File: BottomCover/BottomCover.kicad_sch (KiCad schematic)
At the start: 88 parts, among them J1 USB_C_Receptacle_USB2.0, J12 SM02B-SRSS-TB(LF)(SN), Q2 A03407, SW1 SW_PUSH, SW10 SW_PUSH, SW11 SW_PUSH, SW12 SW_PUSH, SW13 SW_PUSH, SW14 SW_PUSH, SW15 SW_PUSH, SW16 SW_PUSH, SW17 SW_PUSH, SW18 SW_PUSH, SW19 SW_PUSH, SW2 SW_PUSH, SW20 SW_PUSH, SW21 SW_PUSH, SW22 SW_PUSH, SW23 SW_PUSH, SW24 SW_PUSH, SW25 Rotary_Encoder_Switch, SW26 SW_PUSH, SW27 SW_PUSH, SW28 SW_PUSH, SW3 SW_PUSH, SW4 SW_PUSH, SW5 SW_PUSH, SW6 SW_PUSH, SW7 SW_PUSH, SW8 SW_PUSH, SW9 SW_PUSH, U1 LN2054Y42AMR, U2 E73-2G4M08S1C, U3 AP2112K-3.3, Y1 32.768kHz

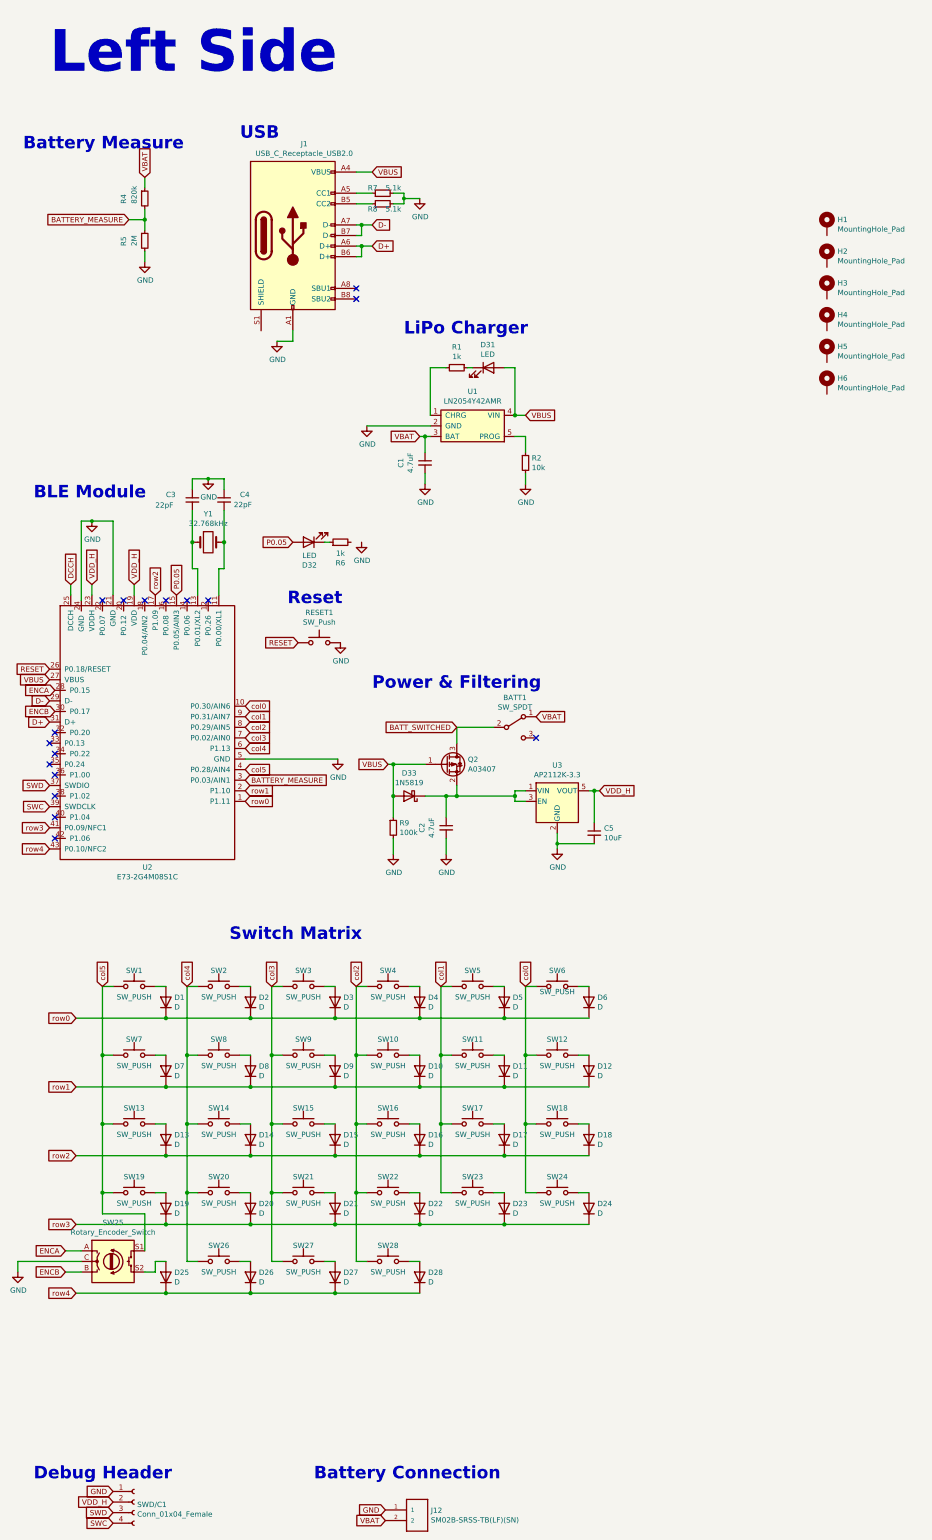
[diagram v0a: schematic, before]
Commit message: minor updates for SMD assembly
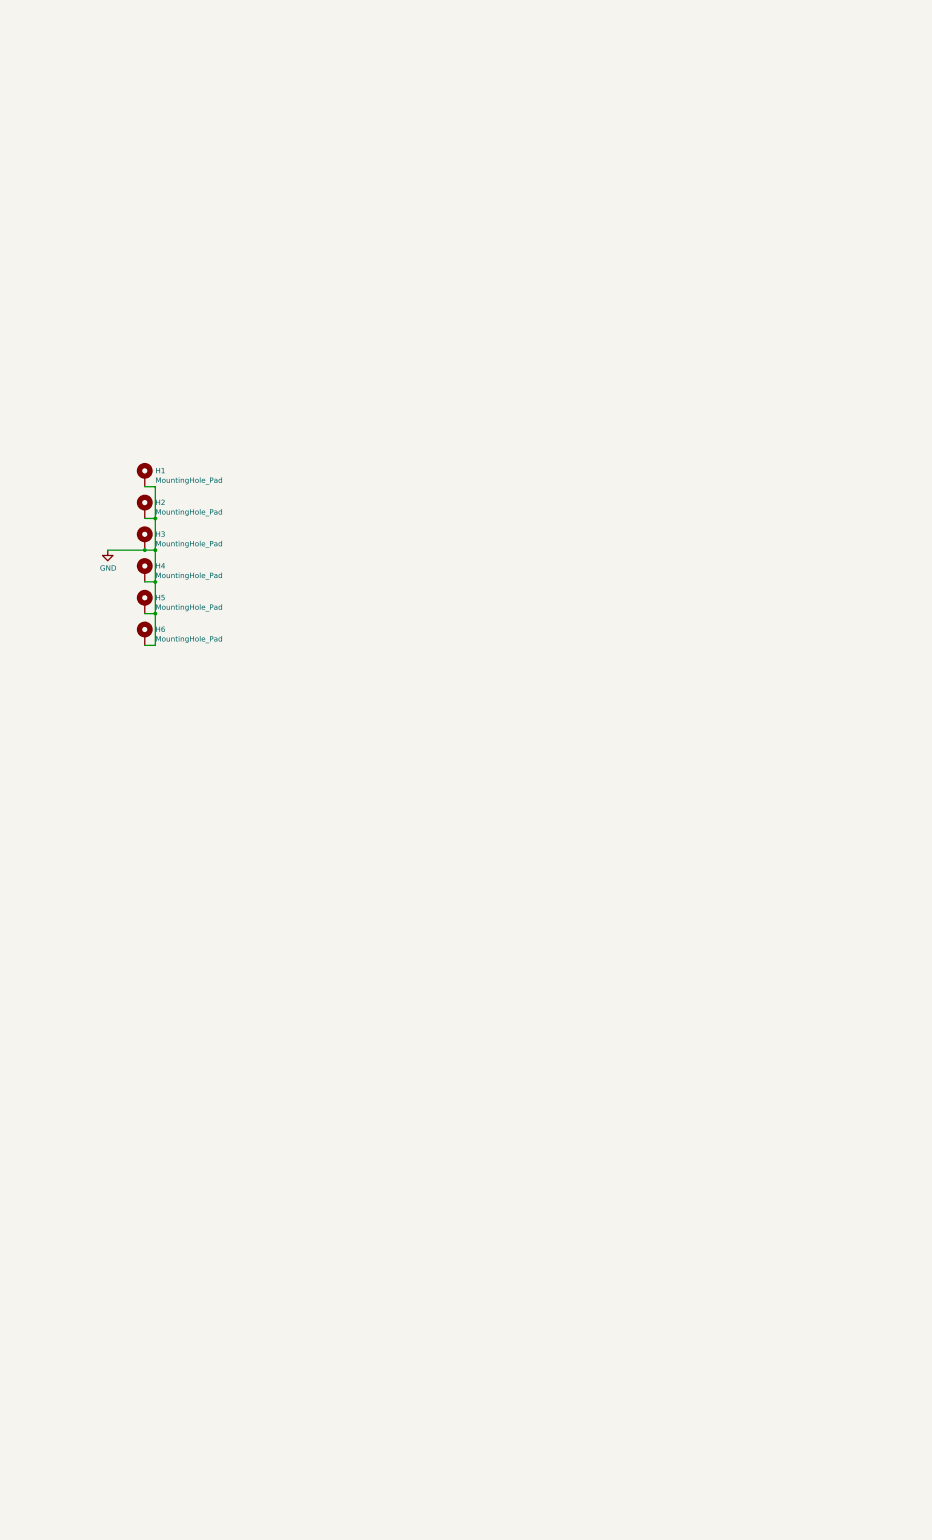
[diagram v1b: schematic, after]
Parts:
- removed BATT1: SW_SPDT, BlueSof:SW-TH_MSK12C02, symbol Switch:SW_SPDT
- removed C1, C2: 4.7uF, Capacitor_SMD:C_0603_1608Metric_Pad1.08x0.95mm_HandSolder, symbol Device:C_Small
- removed C3, C4: 22pF, Capacitor_SMD:C_0603_1608Metric_Pad1.08x0.95mm_HandSolder, symbol Device:C_Small
- removed C5: 10uF, Capacitor_SMD:C_0603_1608Metric_Pad1.08x0.95mm_HandSolder, symbol Device:C_Small
- removed D1, D10, D11, D12, D13, D14, D15, D16, D17, D18, D19, D2, D20, D21, D22, D23, D24, D25, D26, D27, D28, D3, D4, D5, D6, D7, D8, D9: D, Diode_SMD:D_SOD-123, symbol Diode:1N4148
- removed D31, D32: LED, LED_SMD:LED_0603_1608Metric_Pad1.05x0.95mm_HandSolder, symbol Device:LED
- removed D33: 1N5819, Diode_SMD:D_SOD-323_HandSoldering, symbol Diode:1N5819
- removed J1: USB_C_Receptacle_USB2.0, BlueSof:USB-C_C168688, symbol Connector:USB_C_Receptacle_USB2.0
- removed J12: SM02B-SRSS-TB(LF)(SN), BlueSof:SM02B-SRSS-TB(LF)(SN), symbol SM02B-SRSS-TB_LF__SN_:SM02B-SRSS-TB(LF)(SN)
- removed Q2: A03407, Package_TO_SOT_SMD:SOT-23, symbol Device:Q_PMOS_GSD
- removed R1, R6: 1k, Resistor_SMD:R_0603_1608Metric_Pad0.98x0.95mm_HandSolder, symbol Device:R_Small
- removed R2: 10k, Resistor_SMD:R_0603_1608Metric_Pad0.98x0.95mm_HandSolder, symbol Device:R_Small
- removed R4: 820k, Resistor_SMD:R_0603_1608Metric_Pad0.98x0.95mm_HandSolder, symbol Device:R_Small
- removed R5: 2M, Resistor_SMD:R_0603_1608Metric_Pad0.98x0.95mm_HandSolder, symbol Device:R_Small
- removed R7, R8: 5.1k, Resistor_SMD:R_0603_1608Metric_Pad0.98x0.95mm_HandSolder, symbol Device:R_Small
- removed R9: 100k, Resistor_SMD:R_0603_1608Metric_Pad0.98x0.95mm_HandSolder, symbol Device:R_Small
- removed RESET1: SW_Push, Button_Switch_SMD:SW_SPST_B3U-1000P, symbol Switch:SW_Push
- removed SW1, SW10, SW11, SW12, SW13, SW14, SW15, SW16, SW17, SW18, SW19, SW2, SW20, SW21, SW22, SW23, SW24, SW27, SW28, SW3, SW4, SW5, SW6, SW7, SW8, SW9: SW_PUSH, BlueSof:KailhLowProfile, symbol Switch:SW_Push
- removed SW25: Rotary_Encoder_Switch, Rotary_Encoder:RotaryEncoder_Alps_EC11E-Switch_Vertical_H20mm, symbol BlueSof:Rotary_Encoder_Switch-Device-SofleKeyboard-rescue
- removed SW26: SW_PUSH, BlueSof:KailhLowProfile_1.5U, symbol Switch:SW_Push
- removed SWD/C1: Conn_01x04_Female, Connector_PinHeader_2.54mm:PinHeader_1x04_P2.54mm_Vertical, symbol Connector:Conn_01x04_Female
- removed U1: LN2054Y42AMR, Package_TO_SOT_SMD:SOT-23-5, symbol BlueSof-rescue:LN2054Y42AMR-ELLOW
- removed U2: E73-2G4M08S1C, BlueSof:E73-2G4M08S1C-52840_minimal_inside_pads, symbol BlueSof:E73-2G4M08S1C
- removed U3: AP2112K-3.3, Package_TO_SOT_SMD:SOT-23-5, symbol Regulator_Linear:AP2112K-3.3
- removed Y1: 32.768kHz, Crystal:Crystal_SMD_MicroCrystal_CM9V-T1A-2Pin_1.6x1.0mm_HandSoldering, symbol Device:Crystal
- H1, H2, H3, H4, H5, H6: footprint MountingHole:MountingHole_4.3mm_M4 -> MountingHole:MountingHole_2.2mm_M2_ISO7380_Pad
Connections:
- net GND: now also H1.1, H2.1, H3.1, H4.1, H5.1, H6.1
- no-connect marks 17 -> 0
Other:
- note removed: "BLE Module"
- note removed: "Battery Connection"
- note removed: "Battery Measure"
- note removed: "Debug Header"
- note removed: "Left Side"
- note removed: "LiPo Charger"
- note removed: "Power & Filtering"
- note removed: "Reset"
- note removed: "Switch Matrix"
- note removed: "USB"
- moved on the sheet: H1, H2, H3, H4, H5, H6
